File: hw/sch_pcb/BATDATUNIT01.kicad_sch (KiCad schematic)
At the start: 109 parts, among them IC1 MAX14502AETL+, J1 USBC_USB4105-GF-A, J22 HEADER_2x03, J4 46436-9327, J9 SD_Card-FPS009-4200-0, Q1 BC817-25, Q2 BC817-25, Q3 BC817-25, Q4 BC817-25, SW3 KMT031, SW3 SKRTLAE010, SW4 KMT031, SW4 SKRTLAE010, U10 ATMEGA1284P-AU, U10 TCA4307, U11 PCF85263A, U12 TMUX1574DYYR, U2 USBLC6-2SC6, U3 FT260Q-T, U4 PCA9541ABS/01, U6 AT24CS64-SSHM, U6 SHT35-DIS, Y1 8 MHz, Y2 ABS07-120-32.768KHZ-T

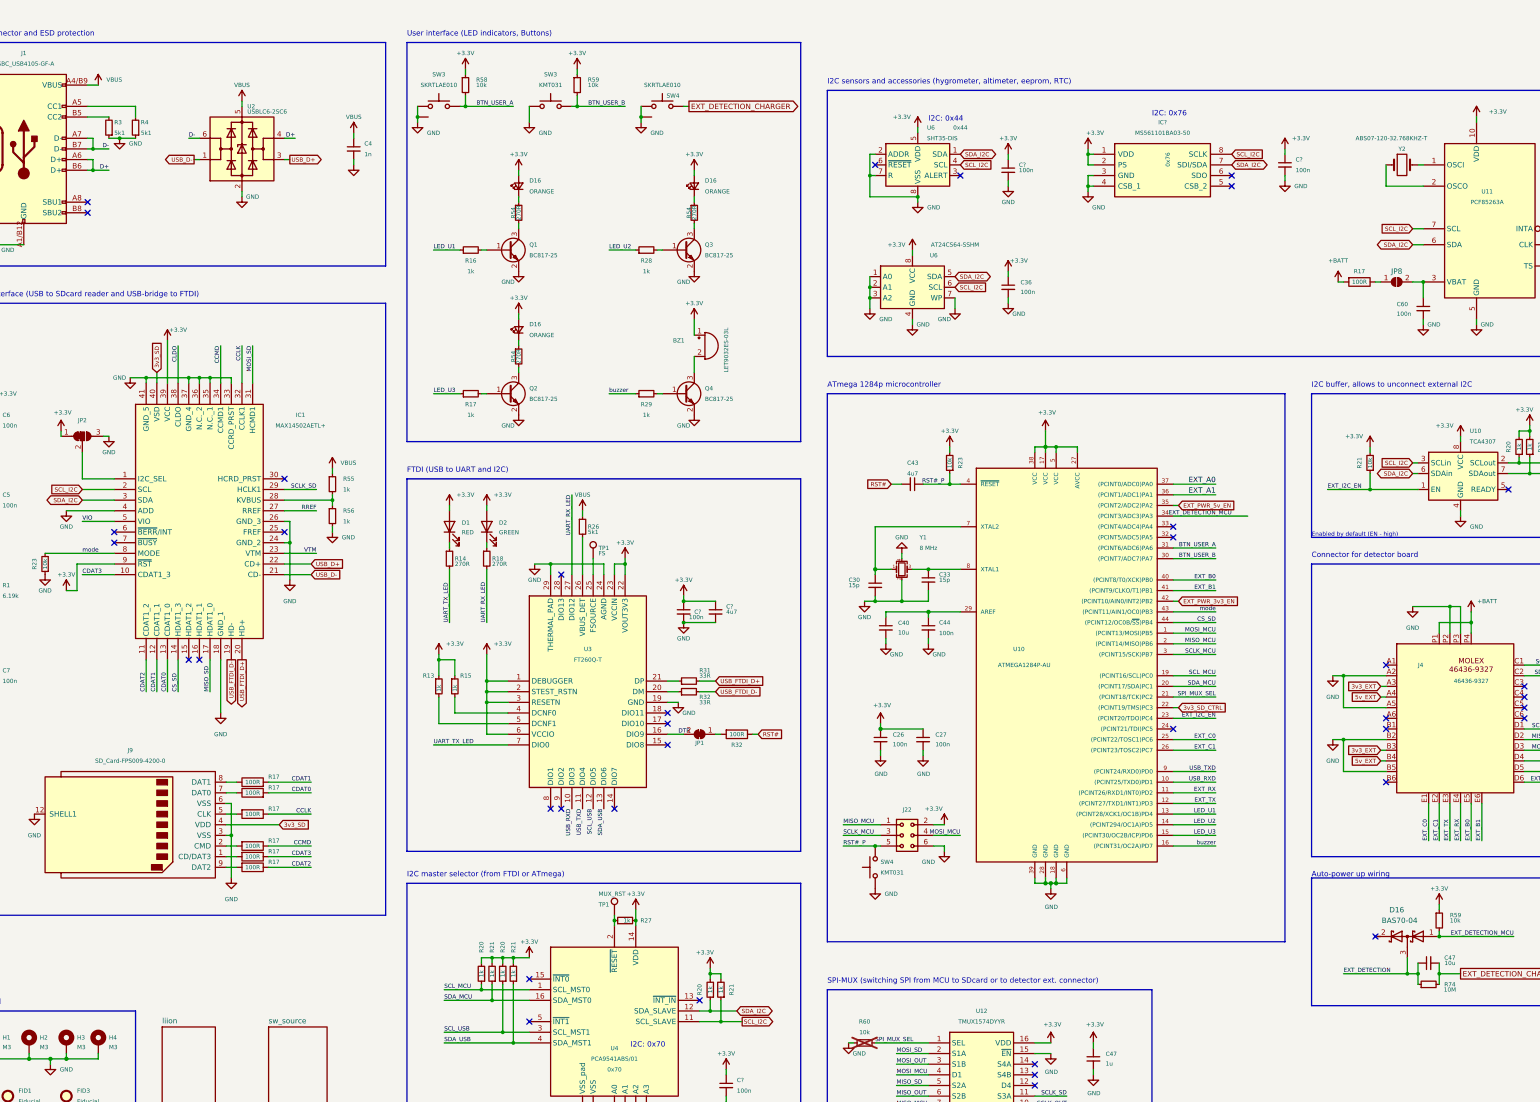
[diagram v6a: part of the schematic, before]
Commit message: update solder jumper to closed
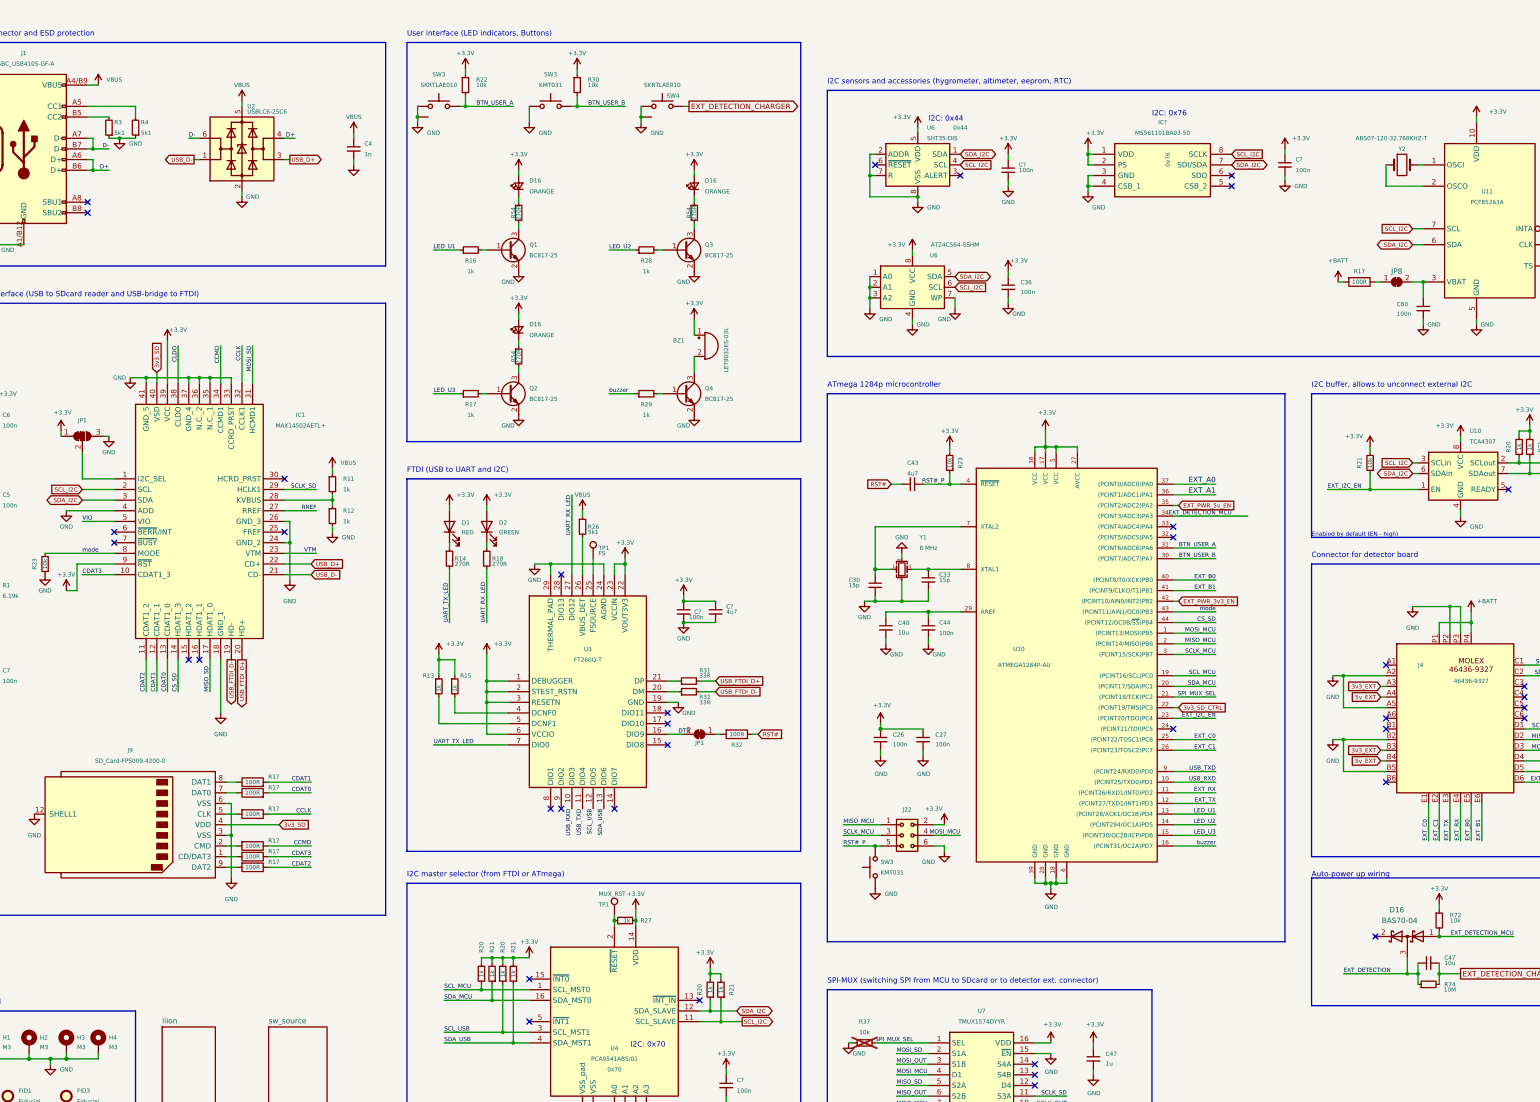
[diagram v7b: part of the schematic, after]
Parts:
- JP8: footprint Jumper:SolderJumper-2_P1.3mm_Open_RoundedPad1.0x1.5mm -> Jumper:SolderJumper-2_P1.3mm_Bridged_RoundedPad1.0x1.5mm; symbol Jumper:SolderJumper_2_Open -> Jumper:SolderJumper_2_Bridged
- renumbered JP2 to JP1, R55 to R11, R56 to R12, R58 to R22, R59 to R30, R60 to R37, R59 to R72, SW4 to SW3, U12 to U7
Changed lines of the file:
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@@
   (symbol (lib_id "Device:R_Small") (at 104.14 133.35 0) (unit 1)
     (in_bom yes) (on_board yes) (dnp no) (fields_autoplaced)
-    (property "Reference" "R56" (at 106.68 132.08 0)
+    (property "Reference" "R12" (at 106.68 132.08 0)
       (effects (font (size 1 1)) (justify left))
     )
@@
   (symbol (lib_id "MLAB_IO:TMUX1574DYYR") (at 246.38 259.08 0) (unit 1)
     (in_bom yes) (on_board yes) (dnp no) (fields_autoplaced)
-    (property "Reference" "U12" (at 259.08 251.46 0)
+    (property "Reference" "U7" (at 259.08 251.46 0)
       (effects (font (size 1 1)))
     )
@@
   (symbol (lib_id "Jumper:SolderJumper_3_Bridged12") (at 44.45 114.3 0) (unit 1)
     (in_bom yes) (on_board yes) (dnp no)
-    (property "Reference" "JP2" (at 44.45 110.49 0)
+    (property "Reference" "JP1" (at 44.45 110.49 0)
       (effects (font (size 1 1)))
     )
@@
   (symbol (lib_id "Device:R_Small") (at 368.3 229.87 0) (unit 1)
     (in_bom yes) (on_board yes) (dnp no)
-    (property "Reference" "R59" (at 370.84 228.6 0)
+    (property "Reference" "R72" (at 370.84 228.6 0)
       (effects (font (size 1 1)) (justify left))
     )
@@
   (symbol (lib_id "Switch:SW_Push") (at 233.68 217.17 90) (unit 1)
     (in_bom yes) (on_board yes) (dnp no) (fields_autoplaced)
-    (property "Reference" "SW4" (at 234.95 215.9 90)
+    (property "Reference" "SW3" (at 234.95 215.9 90)
       (effects (font (size 1 1)) (justify right))
     )
@@
   (symbol (lib_id "power:+3.3V") (at 135.89 26.67 0) (unit 1)
     (in_bom yes) (on_board yes) (dnp no)
-    (property "Reference" "#PWR0109" (at 135.89 30.48 0)
+    (property "Reference" "#PWR031" (at 135.89 30.48 0)
       (effects (font (size 1 1)) hide)
     )
@@
   (symbol (lib_id "power:GND") (at 104.14 137.16 0) (unit 1)
     (in_bom yes) (on_board yes) (dnp no)
-    (property "Reference" "#PWR0101" (at 104.14 143.51 0)
+    (property "Reference" "#PWR024" (at 104.14 143.51 0)
       (effects (font (size 1 1)) hide)
     )
@@
   (symbol (lib_id "power:+3.3V") (at 162.56 26.67 0) (unit 1)
     (in_bom yes) (on_board yes) (dnp no)
-    (property "Reference" "#PWR0110" (at 162.56 30.48 0)
+    (property "Reference" "#PWR044" (at 162.56 30.48 0)
       (effects (font (size 1 1)) hide)
     )
@@
   (symbol (lib_id "power:+3.3V") (at 368.3 226.06 0) (unit 1)
     (in_bom yes) (on_board yes) (dnp no)
-    (property "Reference" "#PWR0110" (at 368.3 229.87 0)
+    (property "Reference" "#PWR0162" (at 368.3 229.87 0)
       (effects (font (size 1 1)) hide)
     )
@@
   (symbol (lib_id "Device:R_Small") (at 135.89 30.48 0) (unit 1)
     (in_bom yes) (on_board yes) (dnp no)
-    (property "Reference" "R58" (at 138.43 29.21 0)
+    (property "Reference" "R22" (at 138.43 29.21 0)
       (effects (font (size 1 1)) (justify left))
     )
@@
   (symbol (lib_id "Device:R_Small") (at 231.14 259.08 90) (unit 1)
     (in_bom no) (on_board yes) (dnp yes) (fields_autoplaced)
-    (property "Reference" "R60" (at 231.14 254 90)
+    (property "Reference" "R37" (at 231.14 254 90)
       (effects (font (size 1 1)))
     )
@@
   (symbol (lib_id "Device:R_Small") (at 104.14 125.73 0) (unit 1)
     (in_bom yes) (on_board yes) (dnp no) (fields_autoplaced)
-    (property "Reference" "R55" (at 106.68 124.46 0)
+    (property "Reference" "R11" (at 106.68 124.46 0)
       (effects (font (size 1 1)) (justify left))
     )
@@
     )
   )
-  (symbol (lib_id "Jumper:SolderJumper_2_Open") (at 358.14 77.47 0) (unit 1)
+  (symbol (lib_id "Jumper:SolderJumper_2_Bridged") (at 358.14 77.47 0) (unit 1)
     (in_bom yes) (on_board yes) (dnp no)
     (property "Reference" "JP8" (at 358.14 74.93 0)
@@
       (effects (font (size 1.27 1.27)) hide)
     )
-    (property "Footprint" "Jumper:SolderJumper-2_P1.3mm_Open_RoundedPad1.0x1.5mm" (at 358.14 77.47 0)
+    (property "Footprint" "Jumper:SolderJumper-2_P1.3mm_Bridged_RoundedPad1.0x1.5mm" (at 358.14 77.47 0)
       (effects (font (size 1.27 1.27)) hide)
     )
@@
   (symbol (lib_id "Device:R_Small") (at 162.56 30.48 0) (unit 1)
     (in_bom yes) (on_board yes) (dnp no)
-    (property "Reference" "R59" (at 165.1 29.21 0)
+    (property "Reference" "R30" (at 165.1 29.21 0)
       (effects (font (size 1 1)) (justify left))
     )
